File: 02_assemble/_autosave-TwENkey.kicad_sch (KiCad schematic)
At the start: 166 parts, among them J1 Conn_01x02, J10 Conn_01x01, J11 Conn_01x01, J12 Conn_01x01, J13 Conn_01x01, J14 Conn_01x01, J15 Conn_01x01, J16 Conn_01x01, J17 Conn_01x01, J18 Conn_01x01, J2 MJ-4PP-9, J3 Conn_01x01, J4 Conn_01x01, J5 Conn_01x01, J6 Conn_01x01, J7 Conn_01x01, J8 Conn_01x01, J9 Conn_01x01, SW1 SW_PUSH, SW10 SW_PUSH, SW11 SW_PUSH, SW12 SW_PUSH, SW13 SW_PUSH, SW14 SW_PUSH, SW15 SW_PUSH, SW16 SW_PUSH, SW17 SW_PUSH, SW18 SW_PUSH, SW19 SW_PUSH, SW2 SW_PUSH, SW20 SW_PUSH, SW21 SW_PUSH, SW22 SW_PUSH, SW23 SW_PUSH, SW24 SW_PUSH, SW25 SW_PUSH, SW26 SW_PUSH, SW27 SW_PUSH, SW28 SW_PUSH, SW29 SW_PUSH, SW3 SW_PUSH, SW30 SW_PUSH, SW31 SW_PUSH, SW32 SW_PUSH, SW33 SW_PUSH, SW34 SW_PUSH, SW35 SW_PUSH, SW36 SW_PUSH, SW37 SW_PUSH, SW38 SW_PUSH, SW39 SW_PUSH, SW4 SW_PUSH, SW40 SW_PUSH, SW41 SW_PUSH, SW42 SW_PUSH, SW43 SW_PUSH, SW44 SW_PUSH, SW45 SW_PUSH, SW46 SW_PUSH, SW47 SW_PUSH, SW48 SW_PUSH, SW49 SW_PUSH, SW5 RotaryEncoder_Switch, SW50 SW_PUSH, SW51 SW_PUSH, SW52 SW_PUSH, SW53 SW_PUSH, SW54 SW_PUSH, SW55 SW_PUSH, SW56 SW_PUSH, SW57 SW_PUSH, SW58 SW_PUSH, SW59 SW_PUSH, SW6 SW_PUSH, SW60 SW_PUSH, SW61 SW_PUSH, SW62 SW_PUSH, SW63 SW_PUSH, SW64 SW_PUSH, SW65 SW_PUSH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

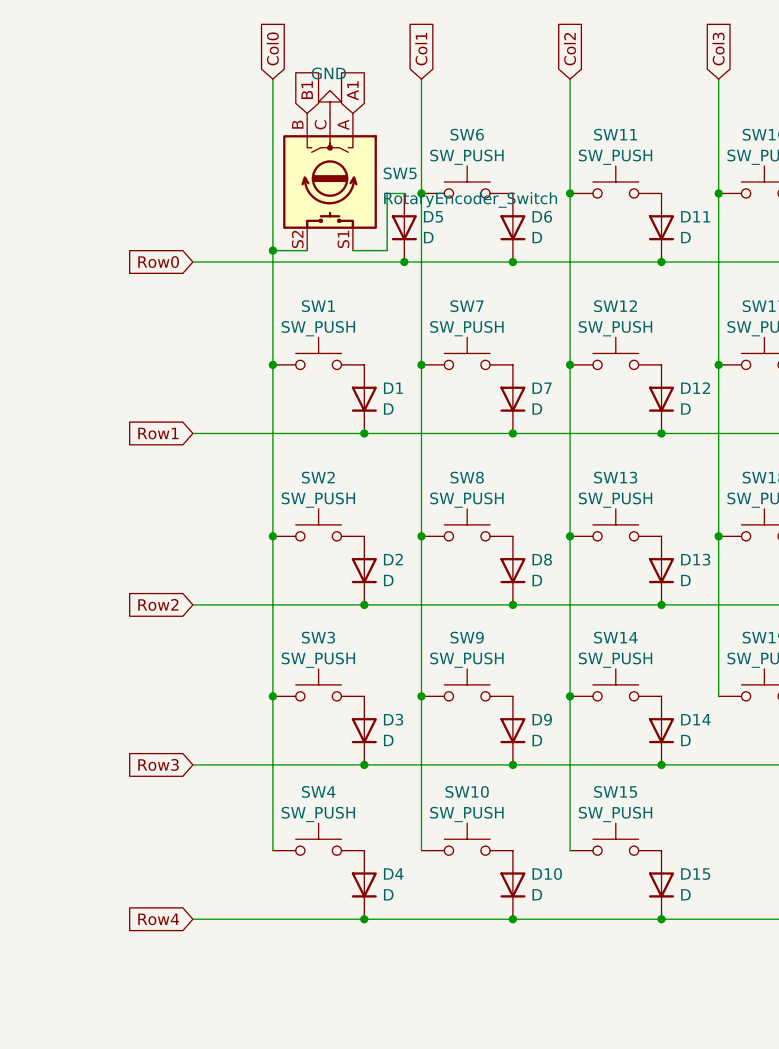
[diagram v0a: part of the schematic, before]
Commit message: TRRSコネクタを追加
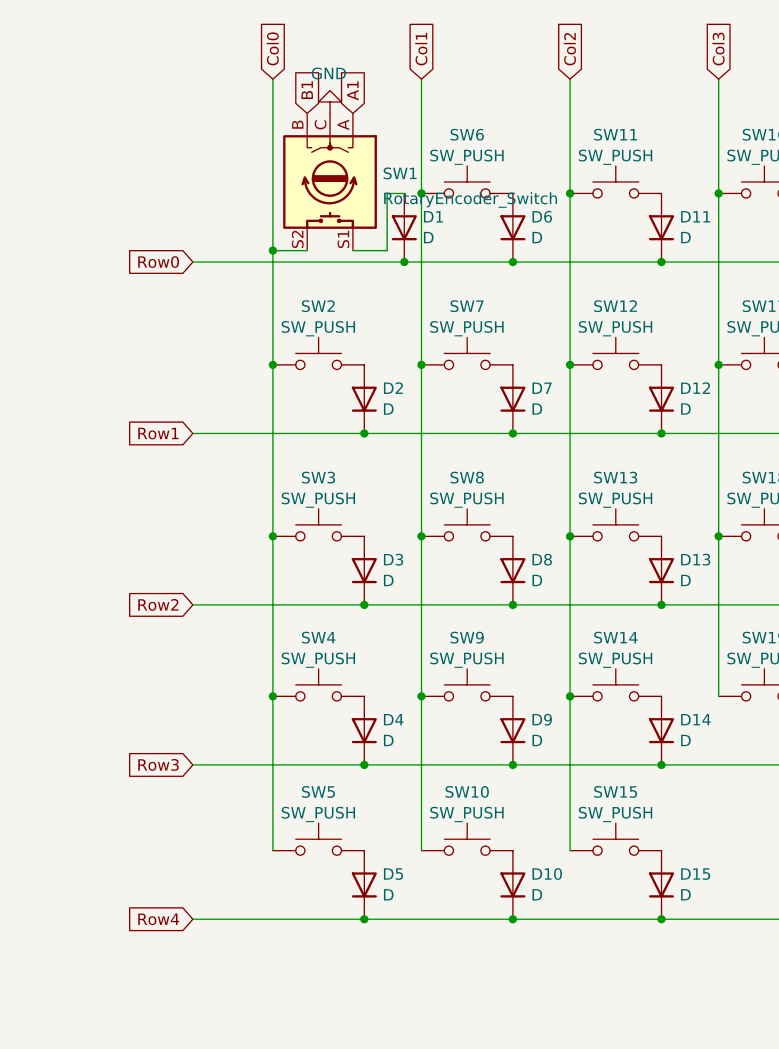
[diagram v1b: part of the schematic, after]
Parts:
- renumbered D5 to D1, D1 to D2, D2 to D3, D3 to D4, D4 to D5, SW5 to SW1, SW1 to SW2, SW2 to SW3, SW3 to SW4, SW4 to SW5
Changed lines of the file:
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@@
   (symbol (lib_id "Switch:SW_Push") (at 54.61 111.125 0) (unit 1)
     (in_bom yes) (on_board yes)
-    (property "Reference" "SW1" (id 0) (at 54.61 104.648 0))
+    (property "Reference" "SW2" (id 0) (at 54.61 104.648 0))
     (property "Value" "SW_PUSH" (id 1) (at 54.61 106.9594 0))
     (property "Footprint" "kbd_SW:CherryMX_Hotswap_1u" (id 2) (at 54.61 111.125 0)
@@
   (symbol (lib_id "Device:D") (at 59.69 114.935 90) (unit 1)
     (in_bom yes) (on_board yes)
-    (property "Reference" "D1" (id 0) (at 61.6966 113.7666 90)
+    (property "Reference" "D2" (id 0) (at 61.6966 113.7666 90)
       (effects (font (size 1.27 1.27)) (justify right))
     )
@@
   (symbol (lib_id "Switch:SW_Push") (at 54.61 130.175 0) (unit 1)
     (in_bom yes) (on_board yes)
-    (property "Reference" "SW2" (id 0) (at 54.61 123.698 0))
+    (property "Reference" "SW3" (id 0) (at 54.61 123.698 0))
     (property "Value" "SW_PUSH" (id 1) (at 54.61 126.0094 0))
     (property "Footprint" "kbd_SW:CherryMX_Hotswap_1u" (id 2) (at 54.61 130.175 0)
@@
   (symbol (lib_id "Switch:SW_Push") (at 54.61 147.955 0) (unit 1)
     (in_bom yes) (on_board yes)
-    (property "Reference" "SW3" (id 0) (at 54.61 141.478 0))
+    (property "Reference" "SW4" (id 0) (at 54.61 141.478 0))
     (property "Value" "SW_PUSH" (id 1) (at 54.61 143.7894 0))
     (property "Footprint" "kbd_SW:CherryMX_Hotswap_1u" (id 2) (at 54.61 147.955 0)
@@
   (symbol (lib_id "Device:D") (at 59.69 133.985 90) (unit 1)
     (in_bom yes) (on_board yes)
-    (property "Reference" "D2" (id 0) (at 61.6966 132.8166 90)
+    (property "Reference" "D3" (id 0) (at 61.6966 132.8166 90)
       (effects (font (size 1.27 1.27)) (justify right))
     )
@@
   (symbol (lib_id "Device:D") (at 59.69 151.765 90) (unit 1)
     (in_bom yes) (on_board yes)
-    (property "Reference" "D3" (id 0) (at 61.6966 150.5966 90)
+    (property "Reference" "D4" (id 0) (at 61.6966 150.5966 90)
       (effects (font (size 1.27 1.27)) (justify right))
     )
@@
   (symbol (lib_id "Switch:SW_Push") (at 54.61 165.1 0) (unit 1)
     (in_bom yes) (on_board yes)
-    (property "Reference" "SW4" (id 0) (at 54.61 158.623 0))
+    (property "Reference" "SW5" (id 0) (at 54.61 158.623 0))
     (property "Value" "SW_PUSH" (id 1) (at 54.61 160.9344 0))
     (property "Footprint" "kbd_SW:CherryMX_Hotswap_1u" (id 2) (at 54.61 165.1 0)
@@
   (symbol (lib_id "Device:D") (at 59.69 168.91 90) (unit 1)
     (in_bom yes) (on_board yes)
-    (property "Reference" "D4" (id 0) (at 61.6966 167.7416 90)
+    (property "Reference" "D5" (id 0) (at 61.6966 167.7416 90)
       (effects (font (size 1.27 1.27)) (justify right))
     )
@@
   (symbol (lib_id "Device:RotaryEncoder_Switch") (at 55.88 90.805 270) (unit 1)
     (in_bom yes) (on_board yes) (fields_autoplaced)
-    (property "Reference" "SW5" (id 0) (at 61.722 89.8965 90)
+    (property "Reference" "SW1" (id 0) (at 61.722 89.8965 90)
       (effects (font (size 1.27 1.27)) (justify left))
     )
@@
   (symbol (lib_id "Device:D") (at 64.135 95.885 90) (unit 1)
     (in_bom yes) (on_board yes)
-    (property "Reference" "D5" (id 0) (at 66.1416 94.7166 90)
+    (property "Reference" "D1" (id 0) (at 66.1416 94.7166 90)
       (effects (font (size 1.27 1.27)) (justify right))
     )
@@
       (reference "#PWR013") (unit 1) (value "GND") (footprint "")
     )
+    (path "/4e06c881-dec3-4ef2-a33d-563ee938f7c1"
+      (reference "D1") (unit 1) (value "D") (footprint "kbd_Parts:Diode_TH_SMD")
+    )
     (path "/00000000-0000-0000-0000-00005bf1727d"
-      (reference "D1") (unit 1) (value "D") (footprint "kbd_Parts:Diode_TH_SMD")
+      (reference "D2") (unit 1) (value "D") (footprint "kbd_Parts:Diode_TH_SMD")
     )
     (path "/00000000-0000-0000-0000-00005c3e5cc1"
-      (reference "D2") (unit 1) (value "D") (footprint "kbd_Parts:Diode_TH_SMD")
+      (reference "D3") (unit 1) (value "D") (footprint "kbd_Parts:Diode_TH_SMD")
     )
     (path "/00000000-0000-0000-0000-00005c3e5db3"
-      (reference "D3") (unit 1) (value "D") (footprint "kbd_Parts:Diode_TH_SMD")
+      (reference "D4") (unit 1) (value "D") (footprint "kbd_Parts:Diode_TH_SMD")
     )
     (path "/00000000-0000-0000-0000-00005c6acff5"
-      (reference "D4") (unit 1) (value "D") (footprint "kbd_Parts:Diode_TH_SMD")
-    )
-    (path "/4e06c881-dec3-4ef2-a33d-563ee938f7c1"
       (reference "D5") (unit 1) (value "D") (footprint "kbd_Parts:Diode_TH_SMD")
     )
@@
       (reference "LED4") (unit 1) (value "LED_SK6812MINI-E") (footprint "kbd_Parts:LED_SK6812MINI-E_BL")
     )
+    (path "/22445357-58ab-411d-a512-980252a33f0a"
+      (reference "SW1") (unit 1) (value "RotaryEncoder_Switch") (footprint "kbd_Parts:RotaryEncoder_EC12E")
+    )
     (path "/00000000-0000-0000-0000-00005bf16f49"
-      (reference "SW1") (unit 1) (value "SW_PUSH") (footprint "kbd_SW:CherryMX_Hotswap_1u")
+      (reference "SW2") (unit 1) (value "SW_PUSH") (footprint "kbd_SW:CherryMX_Hotswap_1u")
     )
     (path "/00000000-0000-0000-0000-00005c3dce20"
-      (reference "SW2") (unit 1) (value "SW_PUSH") (footprint "kbd_SW:CherryMX_Hotswap_1u")
+      (reference "SW3") (unit 1) (value "SW_PUSH") (footprint "kbd_SW:CherryMX_Hotswap_1u")
     )
     (path "/00000000-0000-0000-0000-00005c3dce96"
-      (reference "SW3") (unit 1) (value "SW_PUSH") (footprint "kbd_SW:CherryMX_Hotswap_1u")
+      (reference "SW4") (unit 1) (value "SW_PUSH") (footprint "kbd_SW:CherryMX_Hotswap_1u")
     )
     (path "/00000000-0000-0000-0000-00005c6ab630"
-      (reference "SW4") (unit 1) (value "SW_PUSH") (footprint "kbd_SW:CherryMX_Hotswap_1u")
-    )
-    (path "/22445357-58ab-411d-a512-980252a33f0a"
-      (reference "SW5") (unit 1) (value "RotaryEncoder_Switch") (footprint "kbd_Parts:RotaryEncoder_EC12E")
+      (reference "SW5") (unit 1) (value "SW_PUSH") (footprint "kbd_SW:CherryMX_Hotswap_1u")
     )
     (path "/00000000-0000-0000-0000-00005bf16d93"
